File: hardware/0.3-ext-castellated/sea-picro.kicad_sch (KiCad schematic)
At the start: 54 parts, among them J1 USB_C_Receptacle_USB2.0, J2 Sea-Picro, Q1 2N7002VC-7, Q2 2N7002VC-7, U1 AP7365-33WG-7, U2 GD25Q64CWIGR, U3 RP2040, U4 74LVC1T45Z6-7, Y1 12MHz

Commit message: update production outputs
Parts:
- C1, C10, C11, C12, C13, C14, C15, C16, C17, C18, C19, C2, C3, C4, C5, C6, C7, C8, C9, F1, J1, Q1, Q2, R1, R10, R11, R12, R13, R14, R15, R16, R17, R2, R3, R4, R5, R6, R7, R8, R9: Substitute (none) -> Y
- D1, U3: Substitute (none) -> N
- D2: Substitute (none) -> Y - Any Pink
- J2: now left out of the parts list
- LOGO1, LOGO2, TP1, TP2, TP3, TP4: DNP DNP -> (none)
- U1: LCSC2 (none) -> C82942; MPN2 (none) -> ME6211C33M5G-N; Manufacturer2 (none) -> MICRONE(Nanjing Micro One Elec); Substitute (none) -> Y - Confirm with Josh
- U2: LCSC2 (none) -> C2940197; MPN2 (none) -> W25Q64JVZPIQ; Manufacturer2 (none) -> Winbond; Substitute (none) -> N
- U4: value 74LVC1T45Z6-7 -> 74LVC1T45; LCSC C441819 -> C352970; MPN  74LVC1T45Z6-7 -> SN74LVC1T45DRLR; Manufacturer Diodes Incorporated -> Texas Instruments; Substitute (none) -> N
- Y1: LCSC2 (none) -> C2149205; MPN2 (none) -> 2TJ412000NYGBC; Manufacturer2 (none) -> JYJE; Substitute (none) -> N

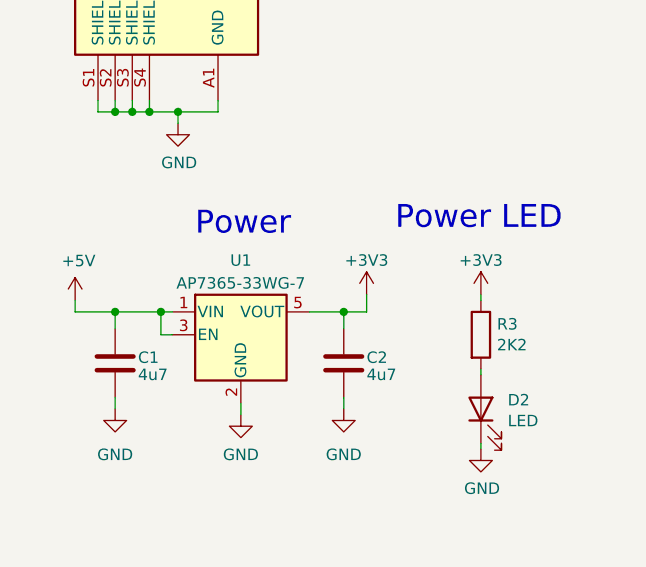
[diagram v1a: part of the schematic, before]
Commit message: add teardrops and melted versions, update LDO MPN
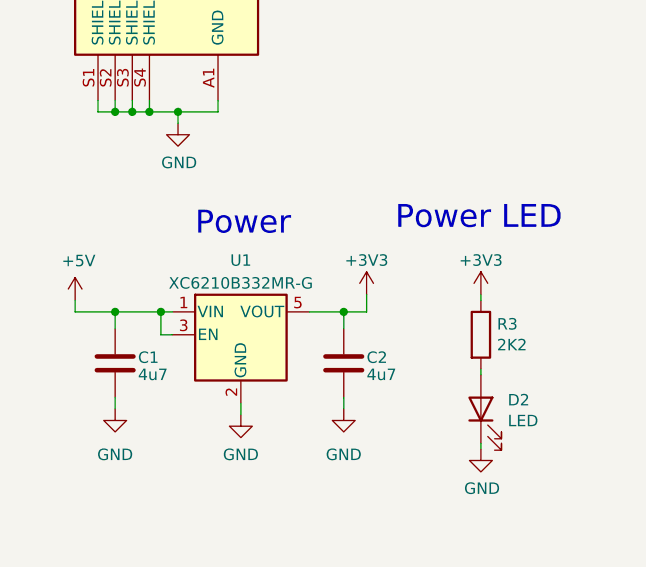
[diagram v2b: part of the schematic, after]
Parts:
- U1: value AP7365-33WG-7 -> XC6210B332MR-G; LCSC C150742 -> C47719; LCSC2 C82942 -> (none); MPN  AP7365-33WG-7 -> XC6210B332MR-G; MPN2 ME6211C33M5G-N -> (none); Manufacturer Diodes Incorporated -> Torex Semiconductor; Manufacturer2 MICRONE(Nanjing Micro One Elec) -> (none); Substitute Y - Confirm with Josh -> N
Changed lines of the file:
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@@
     (in_bom yes) (on_board yes)
     (property "Reference" "U1" (id 0) (at 42.545 86.995 0))
-    (property "Value" "AP7365-33WG-7 " (id 1) (at 42.545 89.535 0))
+    (property "Value" "XC6210B332MR-G" (id 1) (at 42.545 89.535 0))
     (property "Footprint" "josh-soic-sot-etc:SOT-23-5" (id 2) (at 42.545 86.995 0)
       (effects (font (size 1.27 1.27)) hide)
@@
       (effects (font (size 1.27 1.27)) hide)
     )
-    (property "LCSC" "C150742" (id 4) (at 42.545 95.25 0)
-      (effects (font (size 1.27 1.27)) hide)
-    )
-    (property "MPN " "AP7365-33WG-7 " (id 5) (at 42.545 95.25 0)
-      (effects (font (size 1.27 1.27)) hide)
-    )
-    (property "Manufacturer" "Diodes Incorporated" (id 6) (at 42.545 95.25 0)
+    (property "LCSC" "C47719" (id 4) (at 42.545 95.25 0)
+      (effects (font (size 1.27 1.27)) hide)
+    )
+    (property "MPN " "XC6210B332MR-G" (id 5) (at 42.545 95.25 0)
+      (effects (font (size 1.27 1.27)) hide)
+    )
+    (property "Manufacturer" "Torex Semiconductor" (id 6) (at 42.545 95.25 0)
       (effects (font (size 1.27 1.27)) hide)
     )
@@
       (effects (font (size 1.27 1.27)) hide)
     )
-    (property "MPN2" "ME6211C33M5G-N" (id 8) (at 42.545 95.25 0)
-      (effects (font (size 1.27 1.27)) hide)
-    )
-    (property "Manufacturer2" "MICRONE(Nanjing Micro One Elec) " (id 9) (at 42.545 95.25 0)
-      (effects (font (size 1.27 1.27)) hide)
-    )
-    (property "LCSC2" "C82942" (id 10) (at 42.545 95.25 0)
-      (effects (font (size 1.27 1.27)) hide)
-    )
-    (property "Substitute" "Y - Confirm with Josh" (id 11) (at 42.545 95.25 0)
+    (property "MPN2" "" (id 8) (at 42.545 95.25 0)
+      (effects (font (size 1.27 1.27)) hide)
+    )
+    (property "Manufacturer2" "" (id 9) (at 42.545 95.25 0)
+      (effects (font (size 1.27 1.27)) hide)
+    )
+    (property "LCSC2" "" (id 10) (at 42.545 95.25 0)
+      (effects (font (size 1.27 1.27)) hide)
+    )
+    (property "Substitute" "N" (id 11) (at 42.545 95.25 0)
       (effects (font (size 1.27 1.27)) hide)
     )
@@
     )
     (path "/d26fce45-c1d6-42bc-931d-972bf3799097"
-      (reference "U1") (unit 1) (value "AP7365-33WG-7 ") (footprint "josh-soic-sot-etc:SOT-23-5")
+      (reference "U1") (unit 1) (value "XC6210B332MR-G") (footprint "josh-soic-sot-etc:SOT-23-5")
     )
     (path "/578f7d98-6025-491f-b2c7-18b0b10fb26e"
